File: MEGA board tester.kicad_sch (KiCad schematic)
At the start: 92 parts, among them J1 Arduino_Mega_Header

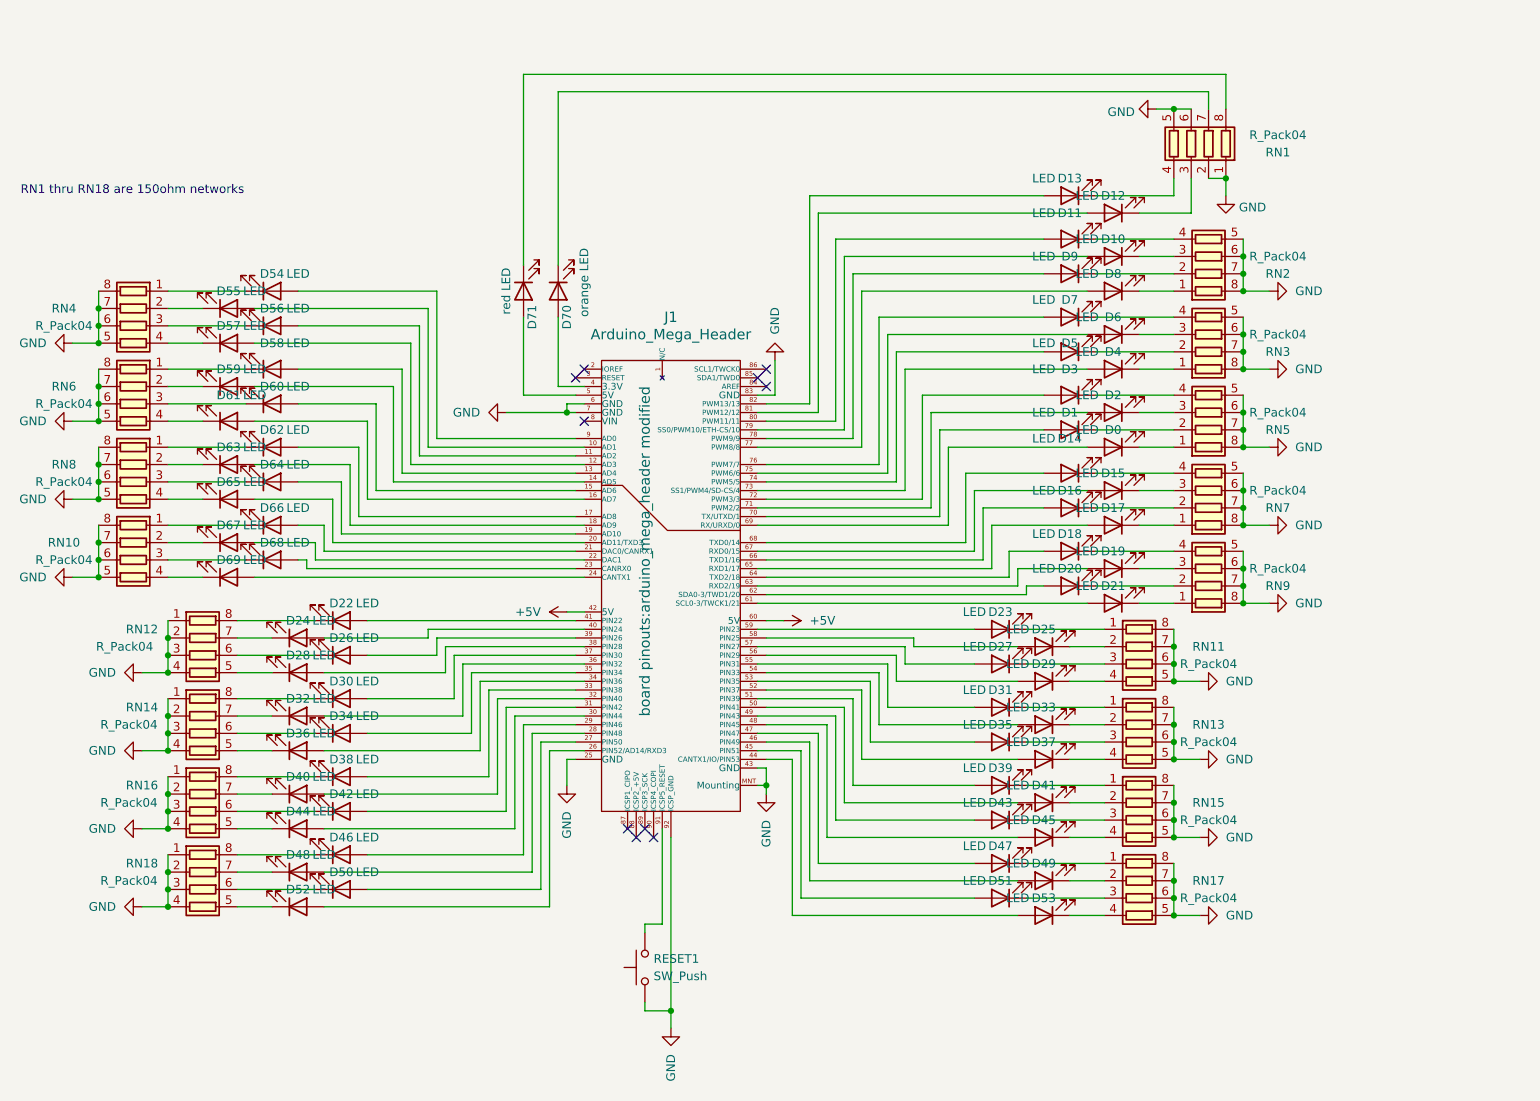
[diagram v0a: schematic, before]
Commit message: PCB, schematic, and code update
PCB update:
- removed the rising sung logo as it was not fab-friendly (was removed by the fab-house from the fab'd PCB)
- updated version to 1.1
- added version and date on User.Drawing layer
- there is a known problem where the data transmission will not happen on arduino if the test board is plugged in, due to pins 0 and 1 (D0 & D1) being used by the board tester. Only (untested) fix for now is to disconnect those two paths from ground by either not populating the pins, or cutting the traces at any point before RN5).

Schematic:
- cleanup. added '150R x4' as value to the resistor networks in place of 'Rpack04'

Code:
- cleanup
- added bit of code to work with Arduino Uno properly, you just need to change `int type = 0` according to which board is being programmed. this needs/will be automated in a future revision.
- added code version and code date at top of code, starting at V1.
- incremented code version at top of code, to V1.1
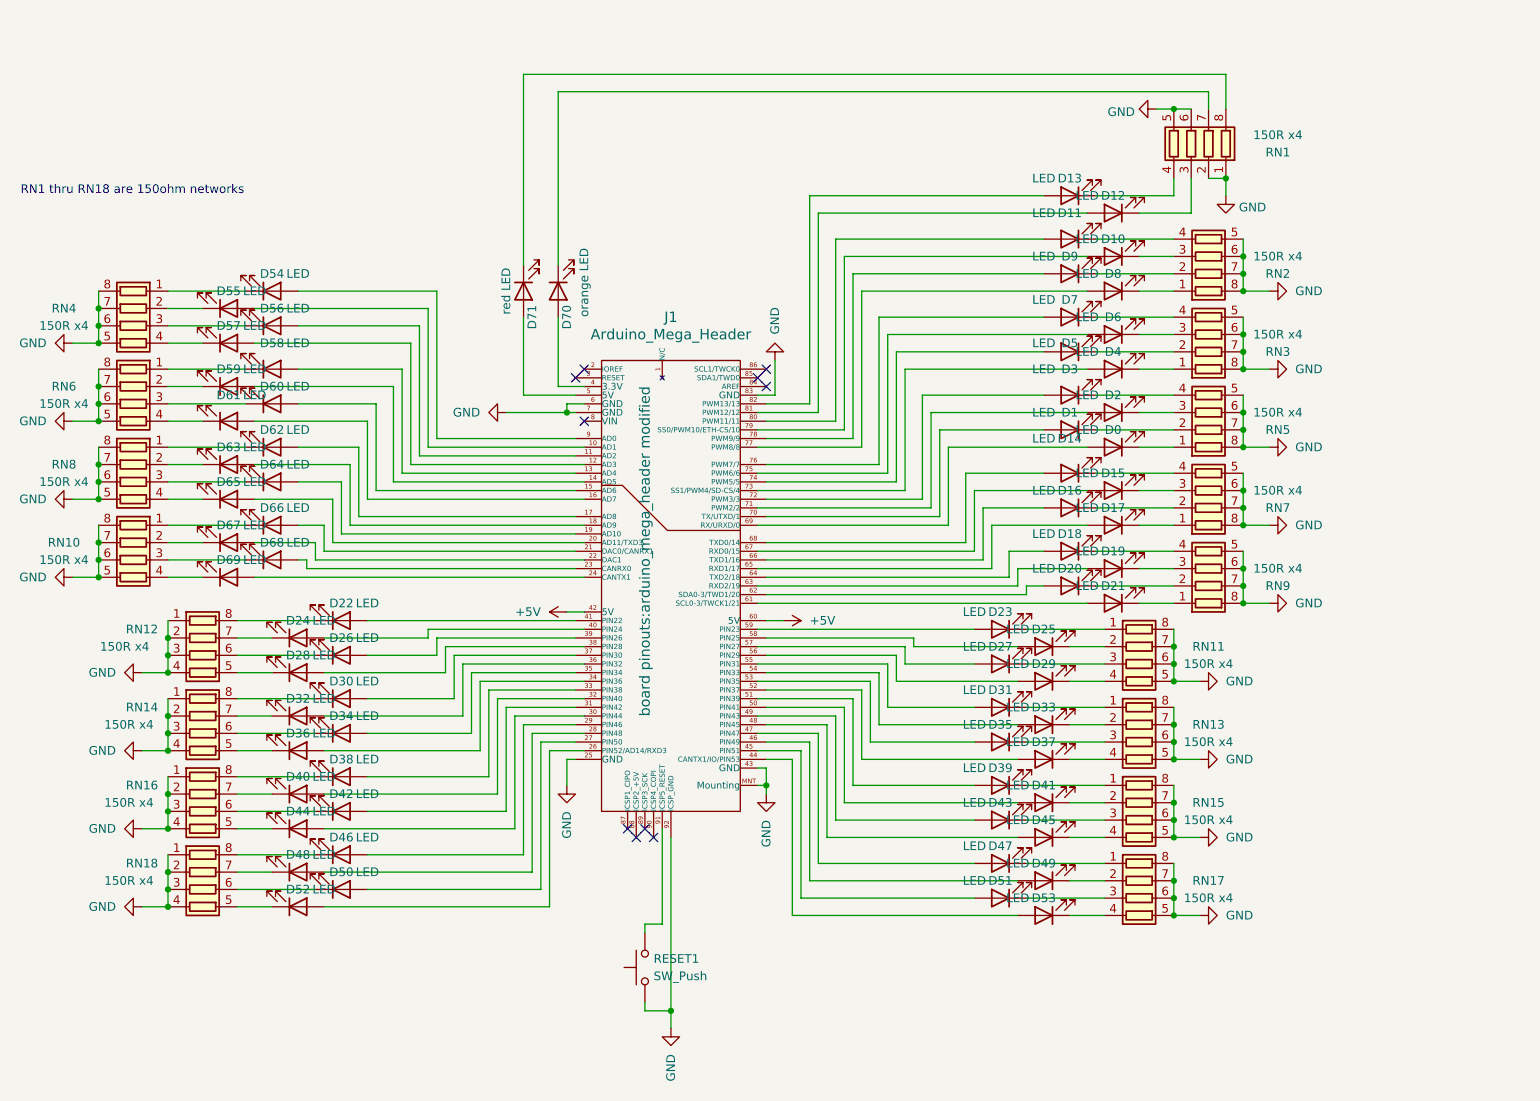
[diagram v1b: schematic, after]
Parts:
- RN1, RN10, RN11, RN12, RN13, RN14, RN15, RN16, RN17, RN18, RN2, RN3, RN4, RN5, RN6, RN7, RN8, RN9: value R_Pack04 -> 150R x4

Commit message: PCB updated to version 2 added  ∅D20, ∅D21, ∅D38, to ensure compatibility with Arduino Zero boards. (D38 is called ANT on the board, unnamed on mega and unoR3) moved the ISTY logo and credits to make place for new components added a QR code linking to the repo on the back updated version on board tweaked placement of a few component names. OCD.
have yet to decide on what to do with D0 and D1 so they don't interfere with program upload. leave them? remove them and put in test loops for probing? tbd.
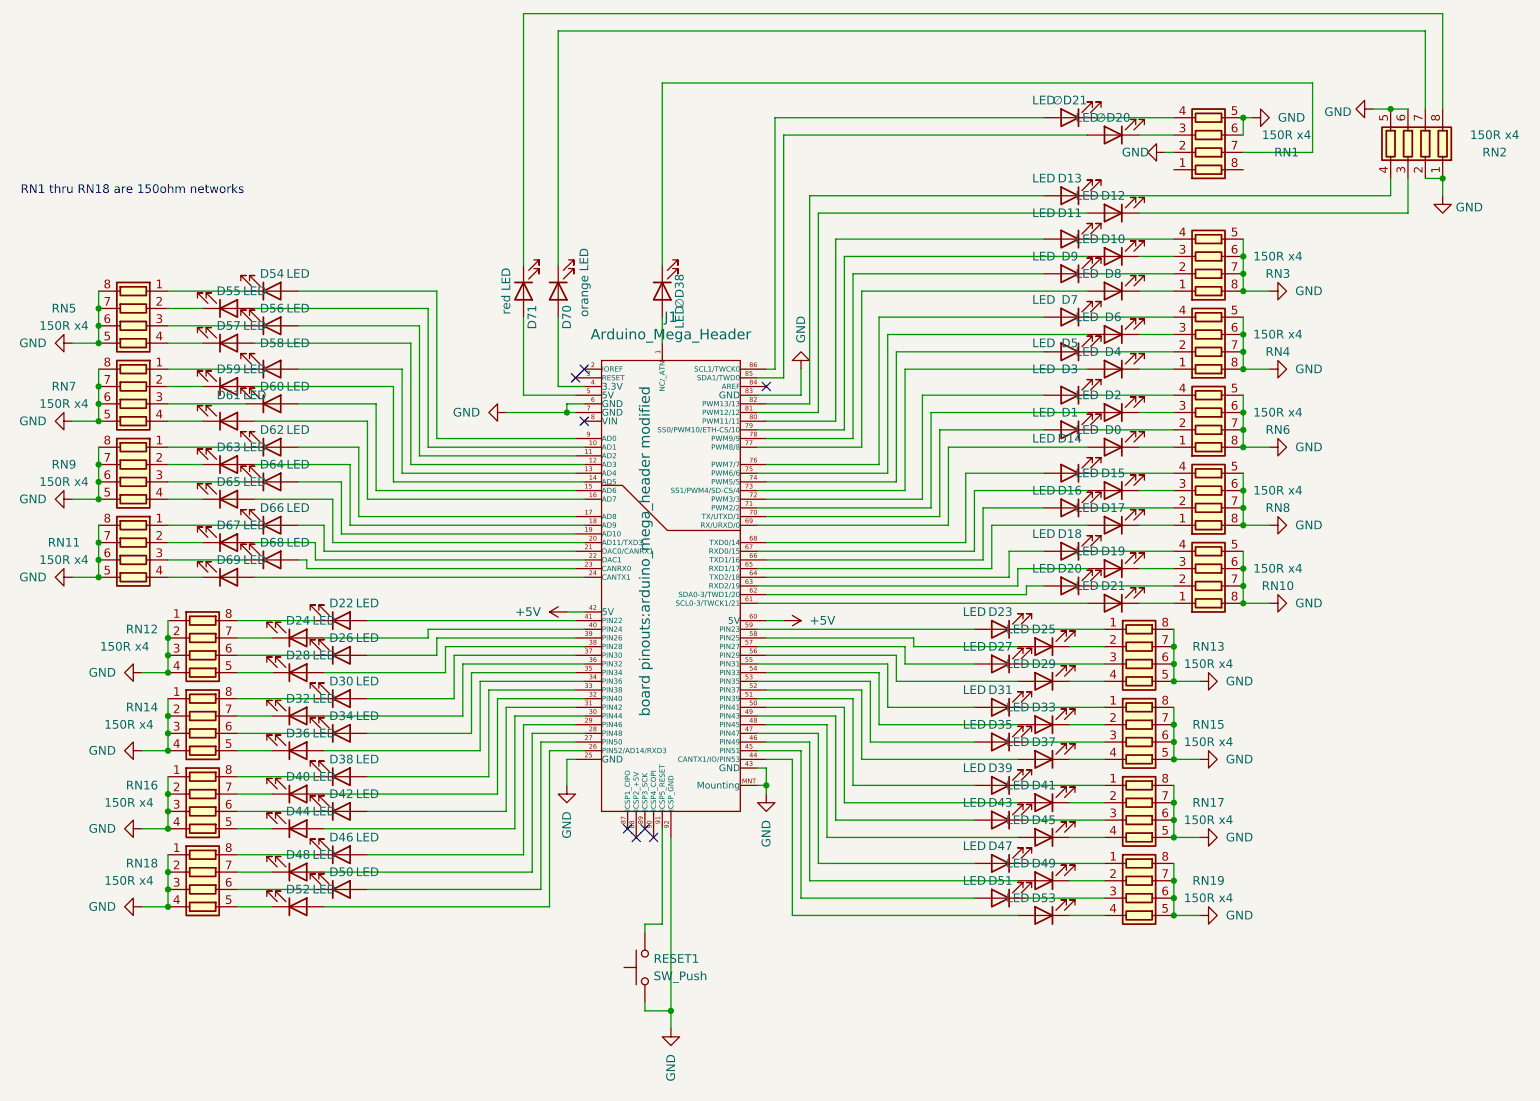
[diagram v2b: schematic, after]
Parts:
- added RN1: 150R x4, Components:R_Array_convex_EXB-S8Vxxxx, symbol Device:R_Pack04
- added ∅D20, ∅D21, ∅D38: LED, Diode_SMD:D_0805_2012Metric_Pad1.15x1.40mm_HandSolder, symbol Device:LED
- RN10: renamed from RN9; footprint components:R_Array_convex_EXB-S8Vxxxx -> Components:R_Array_convex_EXB-S8Vxxxx
- RN11: renamed from RN10; footprint components:R_Array_convex_EXB-S8Vxxxx -> Components:R_Array_convex_EXB-S8Vxxxx
- RN12, RN14, RN16, RN18: footprint components:R_Array_convex_EXB-S8Vxxxx -> Components:R_Array_convex_EXB-S8Vxxxx
- RN13: renamed from RN11; footprint components:R_Array_convex_EXB-S8Vxxxx -> Components:R_Array_convex_EXB-S8Vxxxx
- RN15: renamed from RN13; footprint components:R_Array_convex_EXB-S8Vxxxx -> Components:R_Array_convex_EXB-S8Vxxxx
- RN17: renamed from RN15; footprint components:R_Array_convex_EXB-S8Vxxxx -> Components:R_Array_convex_EXB-S8Vxxxx
- RN19: renamed from RN17; footprint components:R_Array_convex_EXB-S8Vxxxx -> Components:R_Array_convex_EXB-S8Vxxxx
- RN2: renamed from RN1; footprint components:R_Array_convex_EXB-S8Vxxxx -> Components:R_Array_convex_EXB-S8Vxxxx
- RN3: renamed from RN2; footprint components:R_Array_convex_EXB-S8Vxxxx -> Components:R_Array_convex_EXB-S8Vxxxx
- RN4: renamed from RN3; footprint components:R_Array_convex_EXB-S8Vxxxx -> Components:R_Array_convex_EXB-S8Vxxxx
- RN5: renamed from RN4; footprint components:R_Array_convex_EXB-S8Vxxxx -> Components:R_Array_convex_EXB-S8Vxxxx
- RN6: renamed from RN5; footprint components:R_Array_convex_EXB-S8Vxxxx -> Components:R_Array_convex_EXB-S8Vxxxx
- RN7: renamed from RN6; footprint components:R_Array_convex_EXB-S8Vxxxx -> Components:R_Array_convex_EXB-S8Vxxxx
- RN8: renamed from RN7; footprint components:R_Array_convex_EXB-S8Vxxxx -> Components:R_Array_convex_EXB-S8Vxxxx
- RN9: renamed from RN8; footprint components:R_Array_convex_EXB-S8Vxxxx -> Components:R_Array_convex_EXB-S8Vxxxx
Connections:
- net GND: now also RN1.2 (R2.1), RN1.5 (R4.2), RN1.6 (R3.2)
- net at J1.1 (NC/_ATN): now also ∅D38.2 (A)
- net at J1.85 (SDA1/TWD0): now also ∅D20.2 (A)
- net at J1.86 (SCL1/TWCK0): now also ∅D21.2 (A)
- new net: RN1.3 (R3.1), ∅D20.1 (K)
- new net: RN1.4 (R4.1), ∅D21.1 (K)
- new net: RN1.7 (R2.2), ∅D38.1 (K)
- no-connect marks 10 -> 8
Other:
- moved on the sheet: RN2
